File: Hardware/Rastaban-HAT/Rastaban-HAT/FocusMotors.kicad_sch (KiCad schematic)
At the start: 6 parts, among them U6 TMC2208_SILENTSTEPSTICK, U7 DRV8838

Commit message: cleanup and changed some names to Rastaban
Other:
- title: Water Quality Monitor -> Rastaban-HAT
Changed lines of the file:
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@@
   (paper "A4")
   (title_block
-    (title "Water Quality Monitor")
+    (title "Rastaban-HAT")
     (rev "1")
     (company "HAN")

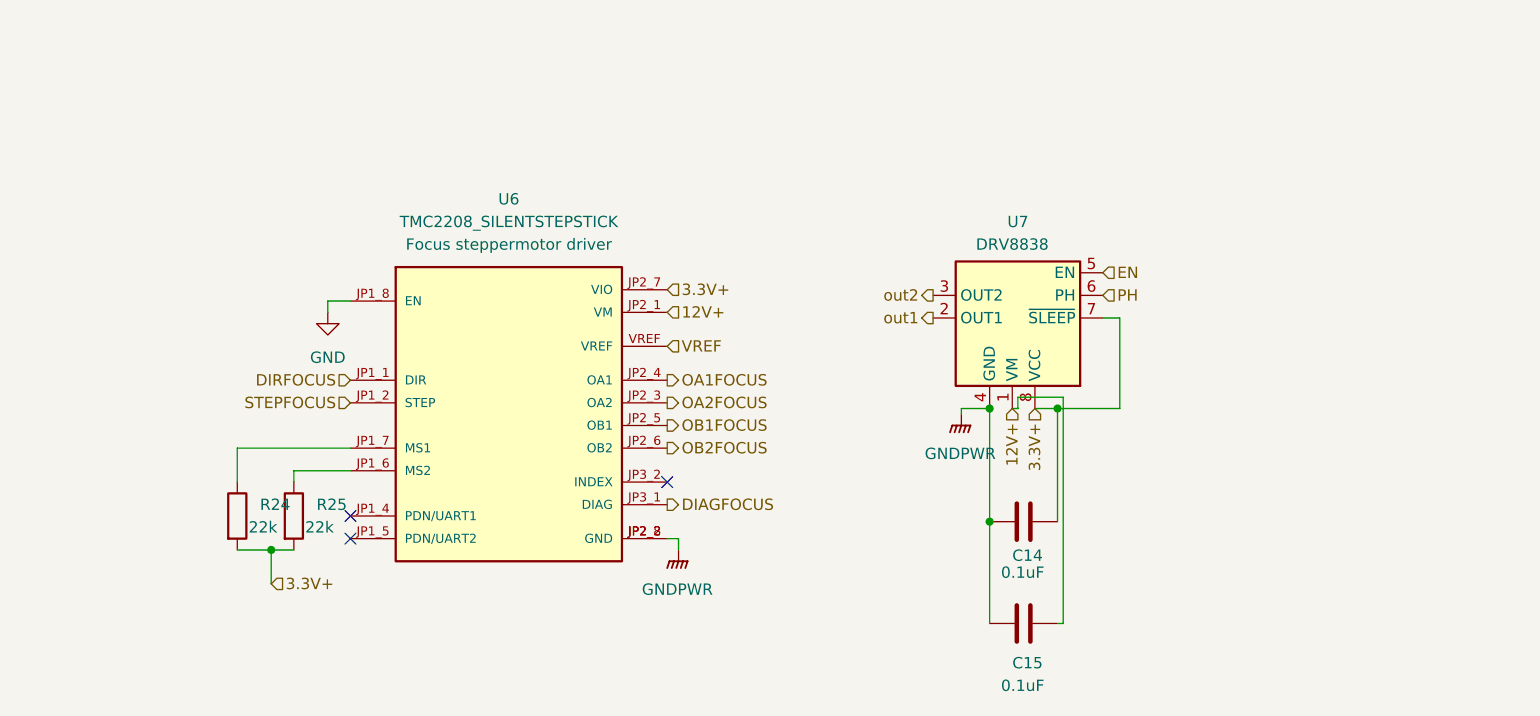
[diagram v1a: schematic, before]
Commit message: updated all ground lables to common ground
switched back from power grounds, since they are not possible (stepper drivers)
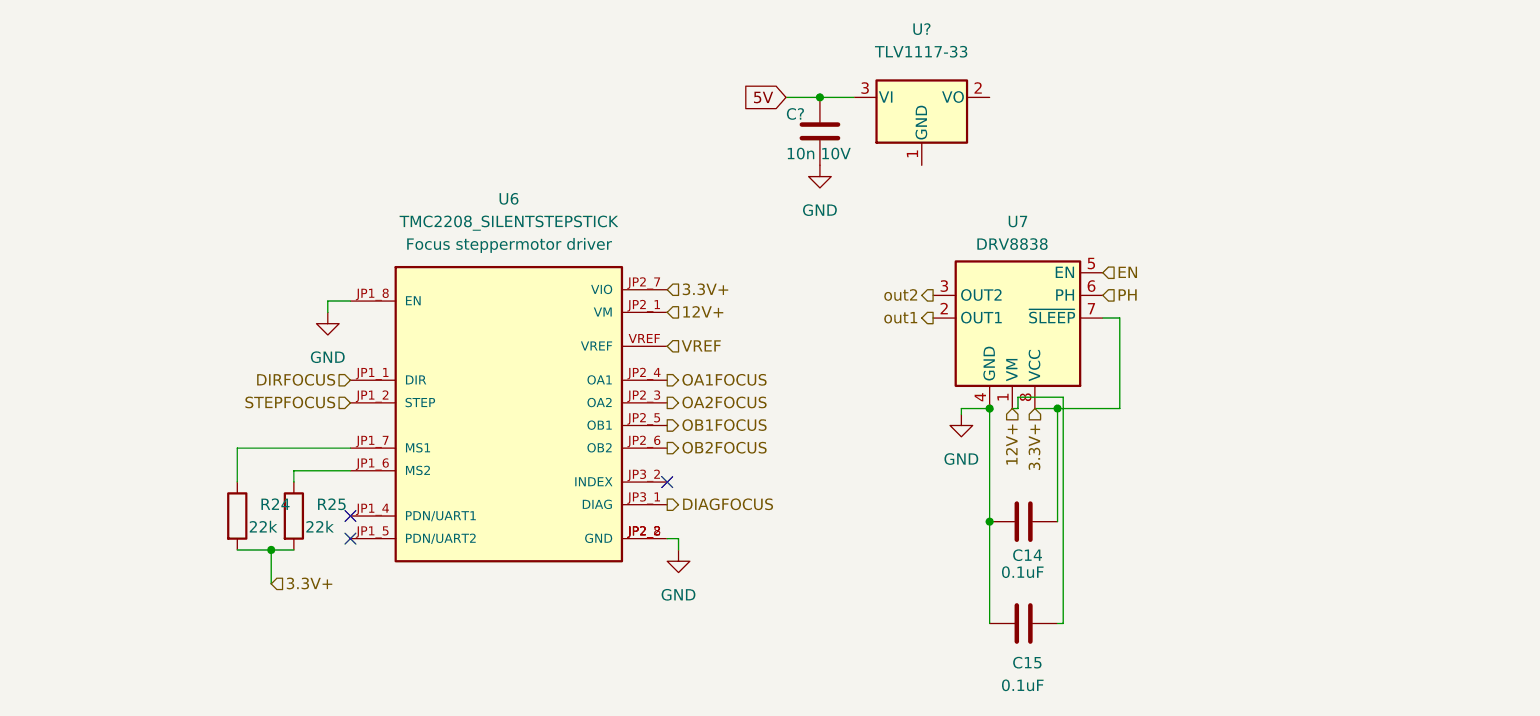
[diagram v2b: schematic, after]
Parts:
- added C?: 10n 10V, symbol Device:C
- added U?: TLV1117-33, symbol Regulator_Linear:TLV1117-33
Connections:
- net GNDPWR is gone; now on net GND: C14.1, C15.1, U6.JP2_2 (GND), U6.JP2_8 (GND), U7.4 (GND), U7.9 (GND)
- net GND: now also C?.2
- new net 5V: C?.1, U?.3 (VI)
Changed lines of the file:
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@@
   (junction (at 177.8 111.125) (diameter 0) (color 0 0 0 0)
+  )
+  (junction (at 158.75 63.5) (diameter 0) (color 0 0 0 0)
   )
   (junction (at 97.155 114.3) (diameter 0) (color 0 0 0 0)
@@
     (stroke (width 0) (type default) (color 0 0 0 0))
   )
+  (wire (pts (xy 154.94 63.5) (xy 158.75 63.5))
+    (stroke (width 0) (type default) (color 0 0 0 0))
+  )
   (wire (pts (xy 174.625 98.425) (xy 177.8 98.425))
     (stroke (width 0) (type default) (color 0 0 0 0))
@@
     (stroke (width 0) (type default) (color 0 0 0 0))
   )
+  (wire (pts (xy 158.75 63.5) (xy 162.56 63.5))
+    (stroke (width 0) (type default) (color 0 0 0 0))
+  )
   (wire (pts (xy 142.875 113.03) (xy 141.605 113.03))
     (stroke (width 0) (type default) (color 0 0 0 0))
@@
     (stroke (width 0) (type default) (color 0 0 0 0))
   )
+  (global_label "5V" (shape input) (at 154.94 63.5 180) (fields_autoplaced)
+    (effects (font (size 1.27 1.27)) (justify right))
+    (property "Intersheet References" "${INTERSHEET_REFS}" (id 0) (at 150.2288 63.5794 0)
+      (effects (font (size 1.27 1.27)) (justify right) hide)
+    )
+  )
   (hierarchical_label "VREF" (shape input) (at 141.605 91.44 0)
     (effects (font (size 1.27 1.27)) (justify left))
@@
     (effects (font (size 1.27 1.27)) (justify right))
   )
-  (symbol (lib_id "power:GNDPWR") (at 142.875 114.3 0) (unit 1)
-    (in_bom yes) (on_board yes) (fields_autoplaced)
-    (property "Reference" "#PWR023" (id 0) (at 142.875 119.38 0)
-      (effects (font (size 1.27 1.27)) hide)
-    )
-    (property "Value" "GNDPWR" (id 1) (at 142.748 118.745 0))
-    (property "Footprint" "" (id 2) (at 142.875 115.57 0)
-      (effects (font (size 1.27 1.27)) hide)
-    )
-    (property "Datasheet" "" (id 3) (at 142.875 115.57 0)
+  (symbol (lib_id "power:GND") (at 174.625 99.06 0) (unit 1)
+    (in_bom yes) (on_board yes) (fields_autoplaced)
+    (property "Reference" "#PWR?" (id 0) (at 174.625 105.41 0)
+      (effects (font (size 1.27 1.27)) hide)
+    )
+    (property "Value" "GND" (id 1) (at 174.625 104.14 0))
+    (property "Footprint" "" (id 2) (at 174.625 99.06 0)
+      (effects (font (size 1.27 1.27)) hide)
+    )
+    (property "Datasheet" "" (id 3) (at 174.625 99.06 0)
       (effects (font (size 1.27 1.27)) hide)
     )
@@
     (pin "VREF")
   )
-  (symbol (lib_id "power:GNDPWR") (at 174.625 99.06 0) (unit 1)
-    (in_bom yes) (on_board yes) (fields_autoplaced)
-    (property "Reference" "#PWR024" (id 0) (at 174.625 104.14 0)
-      (effects (font (size 1.27 1.27)) hide)
-    )
-    (property "Value" "GNDPWR" (id 1) (at 174.498 103.505 0))
-    (property "Footprint" "" (id 2) (at 174.625 100.33 0)
-      (effects (font (size 1.27 1.27)) hide)
-    )
-    (property "Datasheet" "" (id 3) (at 174.625 100.33 0)
-      (effects (font (size 1.27 1.27)) hide)
-    )
-    (pin "1")
-  )
   (symbol (lib_id "Device:C") (at 181.61 122.555 90) (unit 1)
     (in_bom yes) (on_board yes)
@@
     (pin "1")
     (pin "2")
+  )
+  (symbol (lib_id "Regulator_Linear:TLV1117-33") (at 170.18 63.5 0) (unit 1)
+    (in_bom yes) (on_board yes) (fields_autoplaced)
+    (property "Reference" "U?" (id 0) (at 170.18 55.88 0))
+    (property "Value" "TLV1117-33" (id 1) (at 170.18 58.42 0))
+    (property "Footprint" "" (id 2) (at 170.18 63.5 0)
+      (effects (font (size 1.27 1.27)) hide)
+    )
+    (property "Datasheet" "http://www.ti.com/lit/ds/symlink/tlv1117.pdf" (id 3) (at 170.18 63.5 0)
+      (effects (font (size 1.27 1.27)) hide)
+    )
+    (pin "1")
+    (pin "2")
+    (pin "3")
   )
   (symbol (lib_id "power:GND") (at 103.505 87.63 0) (unit 1)
@@
     (pin "2")
   )
+  (symbol (lib_id "power:GND") (at 158.75 71.12 0) (unit 1)
+    (in_bom yes) (on_board yes) (fields_autoplaced)
+    (property "Reference" "#PWR?" (id 0) (at 158.75 77.47 0)
+      (effects (font (size 1.27 1.27)) hide)
+    )
+    (property "Value" "GND" (id 1) (at 158.75 76.2 0))
+    (property "Footprint" "" (id 2) (at 158.75 71.12 0)
+      (effects (font (size 1.27 1.27)) hide)
+    )
+    (property "Datasheet" "" (id 3) (at 158.75 71.12 0)
+      (effects (font (size 1.27 1.27)) hide)
+    )
+    (pin "1")
+  )
+  (symbol (lib_id "power:GND") (at 142.875 114.3 0) (unit 1)
+    (in_bom yes) (on_board yes) (fields_autoplaced)
+    (property "Reference" "#PWR?" (id 0) (at 142.875 120.65 0)
+      (effects (font (size 1.27 1.27)) hide)
+    )
+    (property "Value" "GND" (id 1) (at 142.875 119.38 0))
+    (property "Footprint" "" (id 2) (at 142.875 114.3 0)
+      (effects (font (size 1.27 1.27)) hide)
+    )
+    (property "Datasheet" "" (id 3) (at 142.875 114.3 0)
+      (effects (font (size 1.27 1.27)) hide)
+    )
+    (pin "1")
+  )
   (symbol (lib_id "Device:R") (at 93.345 110.49 0) (unit 1)
     (in_bom yes) (on_board yes)
@@
       (effects (font (size 1.27 1.27)) hide)
     )
+    (pin "1")
+    (pin "2")
+  )
+  (symbol (lib_id "Device:C") (at 158.75 67.31 0) (unit 1)
+    (in_bom yes) (on_board yes)
+    (property "Reference" "C?" (id 0) (at 154.94 65.405 0)
+      (effects (font (size 1.27 1.27)) (justify left))
+    )
+    (property "Value" "10n 10V" (id 1) (at 154.94 69.85 0)
+      (effects (font (size 1.27 1.27)) (justify left))
+    )
+    (property "Footprint" "" (id 2) (at 159.7152 71.12 0)
+      (effects (font (size 1.27 1.27)) hide)
+    )
+    (property "Datasheet" "~" (id 3) (at 158.75 67.31 0)
+      (effects (font (size 1.27 1.27)) hide)
+    )

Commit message: focus motor schematic enh
implemented jeroen's advice
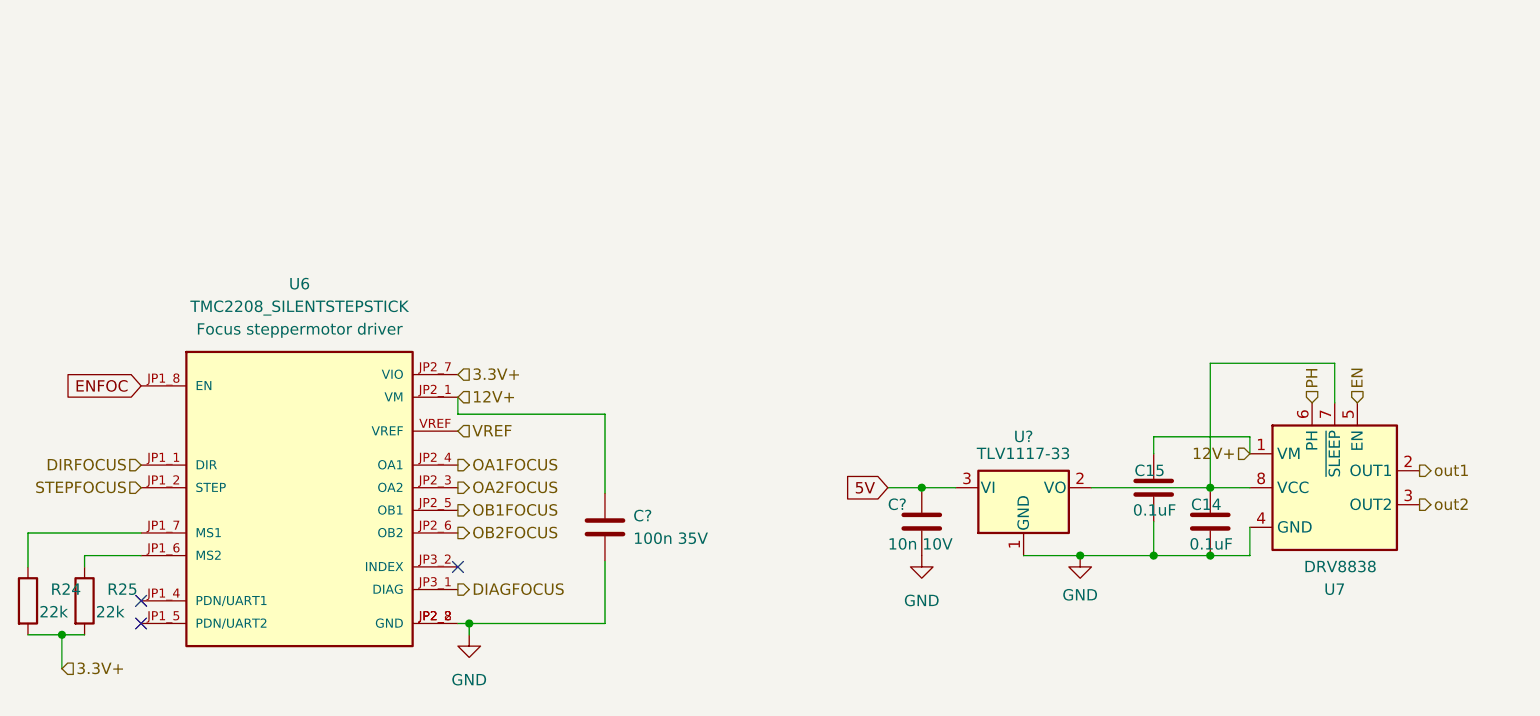
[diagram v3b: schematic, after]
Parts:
- added C?: 100n 35V, symbol Device:C
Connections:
- net 12V+: now also C15.1, C?.1; no longer C15.2
- net 3.3V+: no longer C14.2, U7.7 (~{SLEEP}), U7.8 (VCC)
- net GND: now also C14.2, C15.2, U?.1 (GND), C?.2; no longer C14.1, C15.1, U6.JP1_8 (EN)
- net at U?.2 (VO): now also C14.1, U7.7 (~{SLEEP}), U7.8 (VCC)
- new net ENFOC: U6.JP1_8 (EN)
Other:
- moved on the sheet: C14, C15, C?, R24, R25, U6, U7, U?

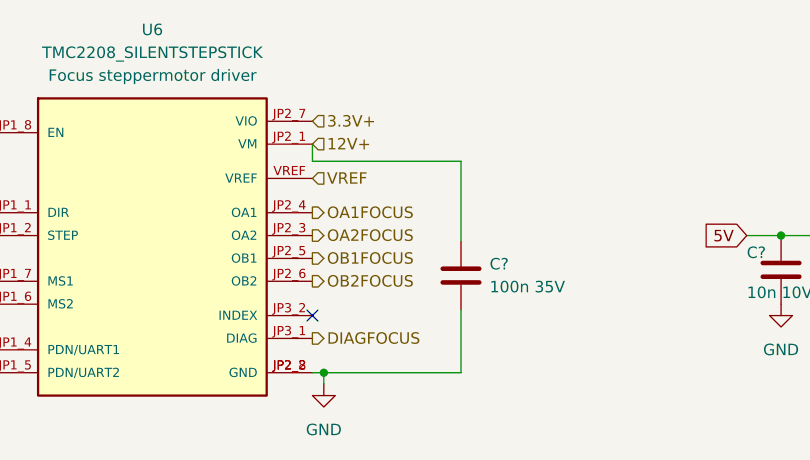
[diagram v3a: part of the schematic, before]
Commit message: enh motor global labels
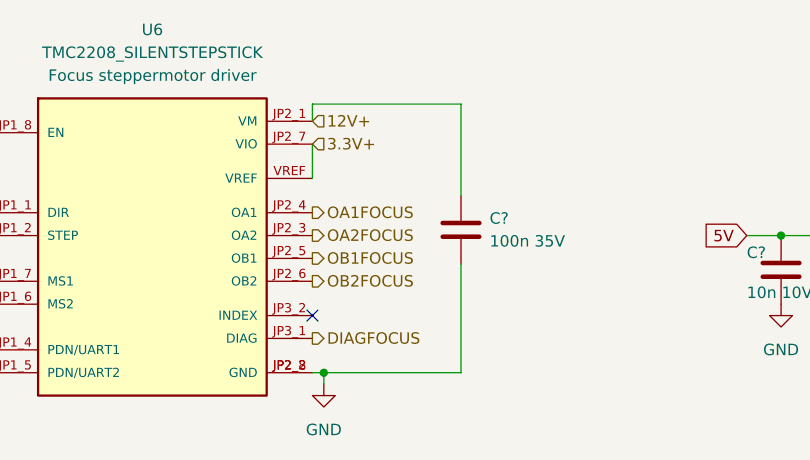
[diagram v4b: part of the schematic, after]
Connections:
- net VREF is gone; now on net 3.3V+: U6.VREF
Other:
- moved on the sheet: C?
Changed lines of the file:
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@@
+    (stroke (width 0) (type default) (color 0 0 0 0))
+  )
+  (wire (pts (xy 118.11 92.71) (xy 118.11 94.615))
     (stroke (width 0) (type default) (color 0 0 0 0))
   )
@@
     (stroke (width 0) (type default) (color 0 0 0 0))
   )
-  (wire (pts (xy 134.62 99.06) (xy 134.62 107.95))
+  (wire (pts (xy 134.62 92.71) (xy 134.62 102.87))
     (stroke (width 0) (type default) (color 0 0 0 0))
   )
@@
     (stroke (width 0) (type default) (color 0 0 0 0))
   )
-  (wire (pts (xy 134.62 115.57) (xy 134.62 122.555))
+  (wire (pts (xy 134.62 110.49) (xy 134.62 122.555))
     (stroke (width 0) (type default) (color 0 0 0 0))
   )
@@
     (stroke (width 0) (type default) (color 0 0 0 0))
   )
-  (wire (pts (xy 118.11 99.06) (xy 134.62 99.06))
-    (stroke (width 0) (type default) (color 0 0 0 0))
-  )
   (wire (pts (xy 187.96 114.935) (xy 196.215 114.935))
     (stroke (width 0) (type default) (color 0 0 0 0))
@@
     (stroke (width 0) (type default) (color 0 0 0 0))
   )
+  (wire (pts (xy 134.62 92.71) (xy 118.11 92.71))
+    (stroke (width 0) (type default) (color 0 0 0 0))
+  )
   (wire (pts (xy 134.62 122.555) (xy 119.38 122.555))
     (stroke (width 0) (type default) (color 0 0 0 0))
   )
-  (wire (pts (xy 118.11 97.155) (xy 118.11 99.06))
-    (stroke (width 0) (type default) (color 0 0 0 0))
-  )
   (wire (pts (xy 69.85 112.395) (xy 69.85 116.205))
+    (stroke (width 0) (type default) (color 0 0 0 0))
+  )
+  (wire (pts (xy 118.11 97.155) (xy 118.11 100.965))
     (stroke (width 0) (type default) (color 0 0 0 0))
   )
@@
     )
   )
-  (hierarchical_label "VREF" (shape input) (at 118.11 100.965 0)
-    (effects (font (size 1.27 1.27)) (justify left))
-  )
   (hierarchical_label "OA2FOCUS" (shape output) (at 118.11 107.315 0)
     (effects (font (size 1.27 1.27)) (justify left))
@@
     (effects (font (size 1.27 1.27)) (justify right))
   )
-  (hierarchical_label "3.3V+" (shape input) (at 118.11 94.615 0)
+  (hierarchical_label "3.3V+" (shape input) (at 118.11 97.155 0)
     (effects (font (size 1.27 1.27)) (justify left))
   )
@@
     (effects (font (size 1.27 1.27)) (justify right))
   )
-  (hierarchical_label "12V+" (shape input) (at 118.11 97.155 0)
+  (hierarchical_label "12V+" (shape input) (at 118.11 94.615 0)
     (effects (font (size 1.27 1.27)) (justify left))
   )
@@
     (pin "2")
   )
-  (symbol (lib_id "Device:C") (at 134.62 111.76 0) (unit 1)
+  (symbol (lib_id "Device:C") (at 134.62 106.68 0) (unit 1)
     (in_bom yes) (on_board yes) (fields_autoplaced)
-    (property "Reference" "C?" (id 0) (at 137.795 110.4899 0)
+    (property "Reference" "C?" (id 0) (at 137.795 105.4099 0)
       (effects (font (size 1.27 1.27)) (justify left))
     )
-    (property "Value" "100n 35V" (id 1) (at 137.795 113.0299 0)
+    (property "Value" "100n 35V" (id 1) (at 137.795 107.9499 0)
       (effects (font (size 1.27 1.27)) (justify left))
     )
-    (property "Footprint" "" (id 2) (at 135.5852 115.57 0)
-      (effects (font (size 1.27 1.27)) hide)
-    )
-    (property "Datasheet" "~" (id 3) (at 134.62 111.76 0)
-      (effects (font (size 1.27 1.27)) hide)
-    )
+    (property "Footprint" "" (id 2) (at 135.5852 110.49 0)
+      (effects (font (size 1.27 1.27)) hide)
+    )
+    (property "Datasheet" "~" (id 3) (at 134.62 106.68 0)
+      (effects (font (size 1.27 1.27)) hide)
+    )
